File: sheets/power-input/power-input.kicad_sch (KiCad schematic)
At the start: 7 parts, among them J1 Eurorack Power

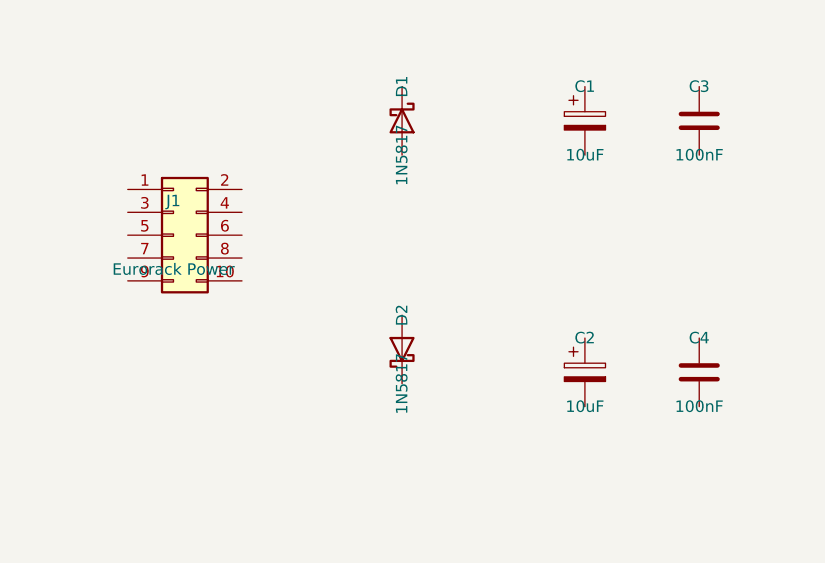
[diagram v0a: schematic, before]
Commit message: Wire the power input sheet
Eurorack 10 pin header, series Schottky protection on both rails, bulk and HF decoupling per rail.

Diode orientation follows current direction: on +12V the anode faces the header and the cathode feeds the rail; on -12V the cathode faces the header, because current flows from the module into the negative supply. ERC cannot check this, so it is stated here.

Rails use global power symbols, not local labels, so the sheet connects to a parent when reused. PWR_FLAG marks each rail as driven, since power arrives through a connector with passive pins.

ERC reports 0 errors and 0 warnings. The layout still needs tidying: labels overlap the header symbol.

D1 and D2 still use the stock Diode:1N5817 symbol. Swap them once 1N5817 exists in the shared library.
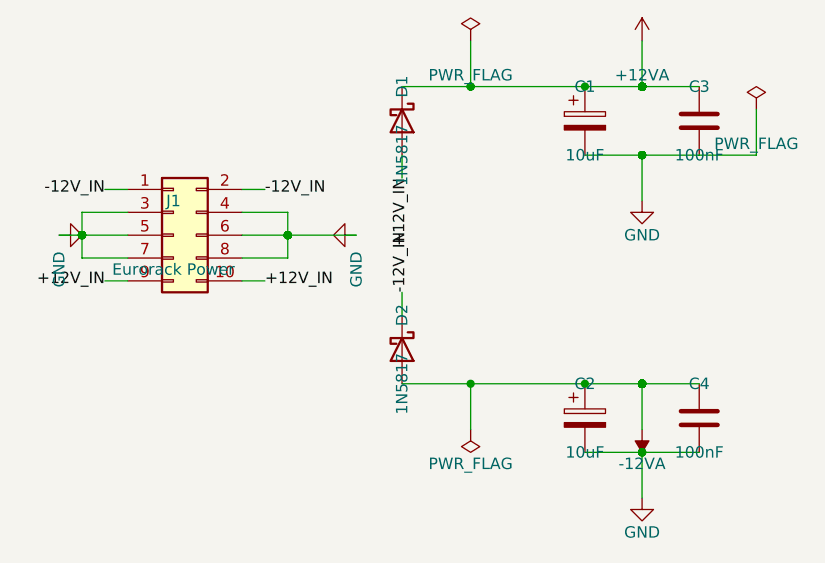
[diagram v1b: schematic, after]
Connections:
- net -12VA: now reaches C4.1
- net -12VA: now also C2.1, D2.2 (A)
- net GND: now reaches C4.2
- net GND: now also C1.2, C2.2, C3.2, J1.3 (Pin_3), J1.4 (Pin_4), J1.5 (Pin_5), J1.6 (Pin_6), J1.7 (Pin_7), J1.8 (Pin_8)
- net +12VA: now reaches C1.1
- net +12VA: now also C3.1, D1.1 (K)
- net +12V_IN: now reaches D1.2 (A)
- net +12V_IN: now also J1.10 (Pin_10), J1.9 (Pin_9)
- net -12V_IN: now reaches D2.1 (K)
- net -12V_IN: now also J1.1 (Pin_1), J1.2 (Pin_2)
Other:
- moved on the sheet: C2, C4, D2
